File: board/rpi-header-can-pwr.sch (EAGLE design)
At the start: 64 parts, among them J1 U.FL, U1 MCP2515, U2 ADS1015, U3 BME280, U4 RFM69HCW, X2 RASPI_BOARD_B+#_E3

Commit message: fixing minor board issues
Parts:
- removed F2: FUSELITTLEFUSE, fuse:FUSELITTLEFUSE
- added F5: FUSETE5, fuse:FUSETE5
- C11, C5, C7: device rcl:C-EUC1206 -> rcl:C-EUC0805
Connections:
- net 5V: now also F5.1; no longer F2.2
- net N$8: now also F5.2; no longer F2.1

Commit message: add in219
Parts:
- removed C13: 100n, rcl:C-EUC0603
- removed C29: 10nF, eagle-ltspice:CC0603
- removed D7: BAS70-04, diode:BAS70-04
- removed R10: 4.7K, resistor:R-EU_R0603
- removed R20: 68k, rcl:R-EU_R0603
- removed R21: 20k, rcl:R-EU_R0603
- removed R22: 1k, rcl:R-EU_R0603
- removed R7: 0, resistor:R-EU_R0603
- removed U2: ADS1015, SparkFun-IC-Conversion:ADS1015
- added C18: 100n, rcl:C-EUC0603
- added R12, R13: 10K, microbuilder:RESISTOR0603
- added R19: 0.1/1% (PT2512FK-070R1L), microbuilder:RESISTOR2512
- added U5: INA219BIDCNT, microbuilder:INA219
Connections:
- removed net 12V_REFERENCE4: D7.C1A2, R20.2, R21.2, R22.1
- removed net ADC_ALERT: R7.1, X2.GPIO21
- removed net ADC_INPUT_1: C29.2, R22.2, U2.AIN0
- removed net N$9: R10.1, R7.2, U2.ALERT/RDY
- new net N$15: R13.2, U5.A1
- new net N$16: R12.2, U5.A0
- new net PRE_SENSE_12V: J3.1, R19.2, U5.VIN+
- new net SCL: U5.SCL
- new net SDA: U5.SDA
- net +12V: no longer R20.1
- net +3V3: now also C18.1, U5.VCC; no longer C13.1, D7.C2, R10.2, U2.VDD
- net GND: now also C18.2, R12.1, R13.1, U5.GND; no longer C13.2, C29.1, D7.A1, R21.1, U2.ADDR, U2.VSS
- net I2C_SCL: no longer U2.SCL
- net I2C_SDA: no longer U2.SDA
- net LORA_DIO0: now also X2.GPIO24; no longer X2.GPIO22
- net LORA_DIO2: now also X2.GPIO22; no longer X2.GPIO24
- net LORA_RST: now also X2.GPIO16; no longer X2.GPIO25
- net PRE_FUSE_12V: now also R19.1, U5.VIN-; no longer J3.1

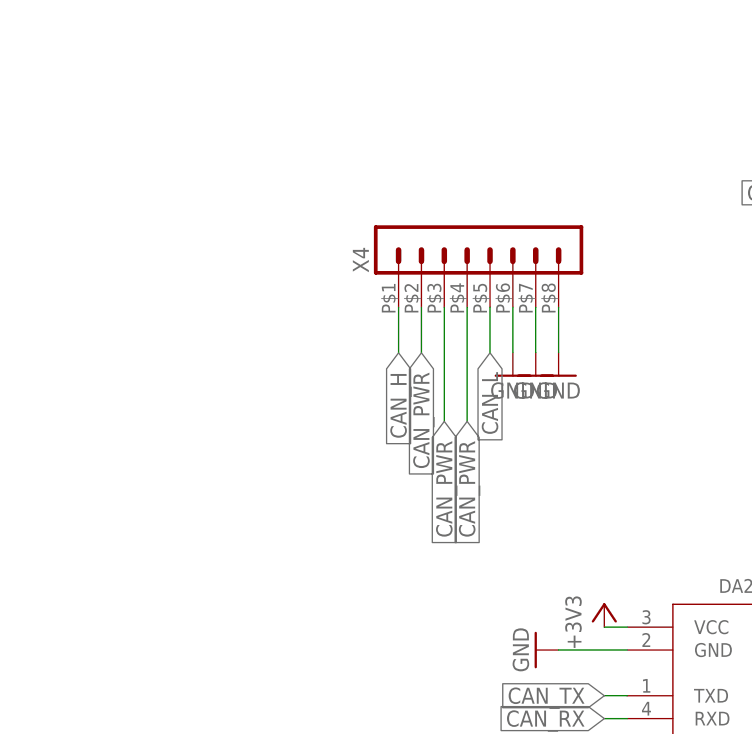
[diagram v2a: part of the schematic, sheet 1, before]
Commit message: change back to rj45 (from microfit)
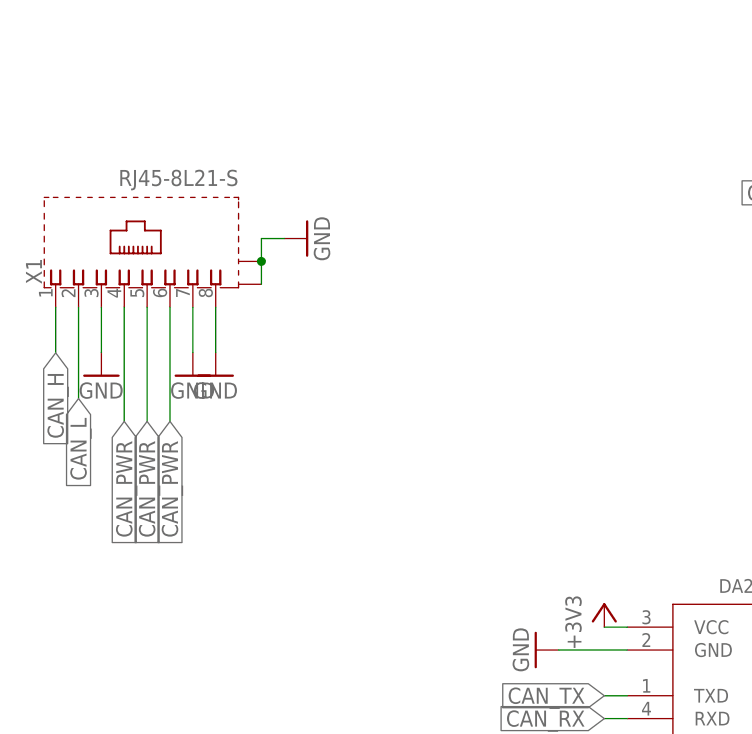
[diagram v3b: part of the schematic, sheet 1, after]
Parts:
- removed X4: (no value), con-molex-micro-fit-3_0:HEADER_POS8_43045-0812
- added X1: RJ45-8L21-S, con-tycoelectronics:RJ45-8L21-S
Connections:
- net CAN_H: now also X1.1; no longer X4.1
- net CAN_L: now also X1.2; no longer X4.5
- net CAN_PWR: now also X1.4, X1.5, X1.6; no longer X4.2, X4.3, X4.4
- net GND: now also X1.3, X1.7, X1.8, X1.S@1, X1.S@2; no longer X4.6, X4.7, X4.8
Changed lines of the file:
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@@
 <part name="C14" library="rcl" deviceset="C-EU" device="C0603" value="1u"/>
 <part name="C15" library="rcl" deviceset="C-EU" device="C0603" value="100n"/>
-<part name="GND23" library="supply1" deviceset="GND" device=""/>
-<part name="GND26" library="supply1" deviceset="GND" device=""/>
-<part name="X4" library="con-molex-micro-fit-3_0" deviceset="HEADER_POS8_?" device="43045-0812"/>
-<part name="GND29" library="supply1" deviceset="GND" device=""/>
 <part name="R11" library="rcl" deviceset="R-EU_" device="R0603" value="120"/>
 <part name="GND17" library="supply1" deviceset="GND" device=""/>
@@
 <part name="C18" library="rcl" deviceset="C-EU" device="C0603" value="100n"/>
 <part name="+3V18" library="supply1" deviceset="+3V3" device=""/>
+<part name="X1" library="con-tycoelectronics" deviceset="RJ45*2" device="1-S" technology="-8L"/>
+<part name="GND28" library="supply1" deviceset="GND" device=""/>
+<part name="GND30" library="supply1" deviceset="GND" device=""/>
+<part name="GND3" library="supply1" deviceset="GND" device=""/>
+<part name="GND19" library="supply1" deviceset="GND" device=""/>
 </parts>
 <sheets>
@@
 <instance part="GND22" gate="1" x="142.24" y="10.16" rot="R90"/>
 <instance part="+3V9" gate="G$1" x="142.24" y="22.86" rot="R270"/>
-<instance part="GND23" gate="1" x="-119.38" y="-20.32"/>
-<instance part="GND26" gate="1" x="-116.84" y="-20.32"/>
-<instance part="X4" gate="G$1" x="-124.46" y="-7.62" rot="R90"/>
-<instance part="GND29" gate="1" x="-121.92" y="-20.32"/>
 <instance part="R11" gate="G$1" x="-76.2" y="0" rot="R180"/>
+<instance part="X1" gate="G$1" x="-162.56" y="-5.08" rot="R90"/>
+<instance part="GND28" gate="1" x="-167.64" y="-20.32"/>
+<instance part="GND30" gate="1" x="-157.48" y="-20.32"/>
+<instance part="GND3" gate="1" x="-154.94" y="-20.32"/>
+<instance part="GND19" gate="1" x="-144.78" y="-5.08" rot="R90"/>
 </instances>
 <busses>
@@
 </segment>
 <segment>
-<wire x1="-119.38" y1="-12.7" x2="-119.38" y2="-17.78" width="0.1524" layer="91"/>
-<pinref part="GND23" gate="1" pin="GND"/>
-<pinref part="X4" gate="G$1" pin="7"/>
-</segment>
-<segment>
-<wire x1="-116.84" y1="-12.7" x2="-116.84" y2="-17.78" width="0.1524" layer="91"/>
-<pinref part="GND26" gate="1" pin="GND"/>
-<pinref part="X4" gate="G$1" pin="8"/>
-</segment>
-<segment>
-<pinref part="X4" gate="G$1" pin="6"/>
-<wire x1="-121.92" y1="-12.7" x2="-121.92" y2="-17.78" width="0.1524" layer="91"/>
-<pinref part="GND29" gate="1" pin="GND"/>
+<pinref part="X1" gate="G$1" pin="3"/>
+<wire x1="-167.64" y1="-12.7" x2="-167.64" y2="-17.78" width="0.1524" layer="91"/>
+<pinref part="GND28" gate="1" pin="GND"/>
+</segment>
+<segment>
+<pinref part="X1" gate="G$1" pin="7"/>
+<wire x1="-157.48" y1="-12.7" x2="-157.48" y2="-17.78" width="0.1524" layer="91"/>
+<pinref part="GND30" gate="1" pin="GND"/>
+</segment>
+<segment>
+<pinref part="X1" gate="G$1" pin="8"/>
+<wire x1="-154.94" y1="-12.7" x2="-154.94" y2="-17.78" width="0.1524" layer="91"/>
+<pinref part="GND3" gate="1" pin="GND"/>
+</segment>
+<segment>
+<pinref part="X1" gate="G$1" pin="S@1"/>
+<pinref part="X1" gate="G$1" pin="S@2"/>
+<wire x1="-149.86" y1="-10.16" x2="-149.86" y2="-7.62" width="0.1524" layer="91"/>
+<wire x1="-149.86" y1="-7.62" x2="-149.86" y2="-5.08" width="0.1524" layer="91"/>
+<junction x="-149.86" y="-7.62"/>
+<wire x1="-149.86" y1="-5.08" x2="-147.32" y2="-5.08" width="0.1524" layer="91"/>
+<pinref part="GND19" gate="1" pin="GND"/>
 </segment>
 </net>
@@
 </segment>
 <segment>
-<wire x1="-134.62" y1="-12.7" x2="-134.62" y2="-17.78" width="0.1524" layer="91"/>
-<label x="-134.62" y="-17.78" size="1.778" layer="95" rot="R270" xref="yes"/>
-<pinref part="X4" gate="G$1" pin="1"/>
-</segment>
-<segment>
 <pinref part="R11" gate="G$1" pin="2"/>
 <wire x1="-81.28" y1="0" x2="-86.36" y2="0" width="0.1524" layer="91"/>
 <label x="-86.36" y="0" size="1.778" layer="95" rot="R180" xref="yes"/>
 </segment>
+<segment>
+<pinref part="X1" gate="G$1" pin="1"/>
+<wire x1="-172.72" y1="-12.7" x2="-172.72" y2="-17.78" width="0.1524" layer="91"/>
+<label x="-172.72" y="-17.78" size="1.778" layer="95" rot="R270" xref="yes"/>
+</segment>
 </net>
 <net name="CAN_L" class="0">
@@
 </segment>
 <segment>
-<pinref part="X4" gate="G$1" pin="5"/>
-<wire x1="-124.46" y1="-12.7" x2="-124.46" y2="-17.78" width="0.1524" layer="91"/>
-<label x="-124.46" y="-17.78" size="1.778" layer="95" rot="R270" xref="yes"/>
-</segment>
-<segment>
 <pinref part="R11" gate="G$1" pin="1"/>
 <wire x1="-66.04" y1="0" x2="-71.12" y2="0" width="0.1524" layer="91"/>
 <label x="-66.04" y="0" size="1.778" layer="95" xref="yes"/>
 </segment>
+<segment>
+<pinref part="X1" gate="G$1" pin="2"/>
+<wire x1="-170.18" y1="-12.7" x2="-170.18" y2="-22.86" width="0.1524" layer="91"/>
+<label x="-170.18" y="-22.86" size="1.778" layer="95" rot="R270" xref="yes"/>
+</segment>
 </net>
 <net name="N$17" class="0">
@@
 <net name="CAN_PWR" class="0">
 <segment>
-<pinref part="X4" gate="G$1" pin="2"/>
-<wire x1="-132.08" y1="-12.7" x2="-132.08" y2="-17.78" width="0.1524" layer="91"/>
-<label x="-132.08" y="-17.78" size="1.778" layer="95" rot="R270" xref="yes"/>
-</segment>
-<segment>
-<pinref part="X4" gate="G$1" pin="3"/>
-<wire x1="-129.54" y1="-12.7" x2="-129.54" y2="-25.4" width="0.1524" layer="91"/>
-<label x="-129.54" y="-25.4" size="1.778" layer="95" rot="R270" xref="yes"/>
-</segment>
-<segment>
-<wire x1="-127" y1="-12.7" x2="-127" y2="-25.4" width="0.1524" layer="91"/>
-<label x="-127" y="-25.4" size="1.778" layer="95" rot="R270" xref="yes"/>
-<pinref part="X4" gate="G$1" pin="4"/>
-</segment>
-<segment>
 <label x="-25.4" y="12.7" size="1.778" layer="95" rot="R180" xref="yes"/>
 <pinref part="F3" gate="G$1" pin="1"/>
 <wire x1="-25.4" y1="12.7" x2="-15.24" y2="12.7" width="0.1524" layer="91"/>
 </segment>
-</net>
+<segment>
+<pinref part="X1" gate="G$1" pin="4"/>
+<wire x1="-165.1" y1="-12.7" x2="-165.1" y2="-25.4" width="0.1524" layer="91"/>
+<label x="-165.1" y="-25.4" size="1.778" layer="95" rot="R270" xref="yes"/>
+</segment>
+<segment>
+<pinref part="X1" gate="G$1" pin="5"/>
+<wire x1="-162.56" y1="-12.7" x2="-162.56" y2="-25.4" width="0.1524" layer="91"/>
+<label x="-162.56" y="-25.4" size="1.778" layer="95" rot="R270" xref="yes"/>
+</segment>
+<segment>
+<pinref part="X1" gate="G$1" pin="6"/>
+<wire x1="-160.02" y1="-12.7" x2="-160.02" y2="-25.4" width="0.1524" layer="91"/>
+<label x="-160.02" y="-25.4" size="1.778" layer="95" rot="R270" xref="yes"/>
+</segment>
+</net>

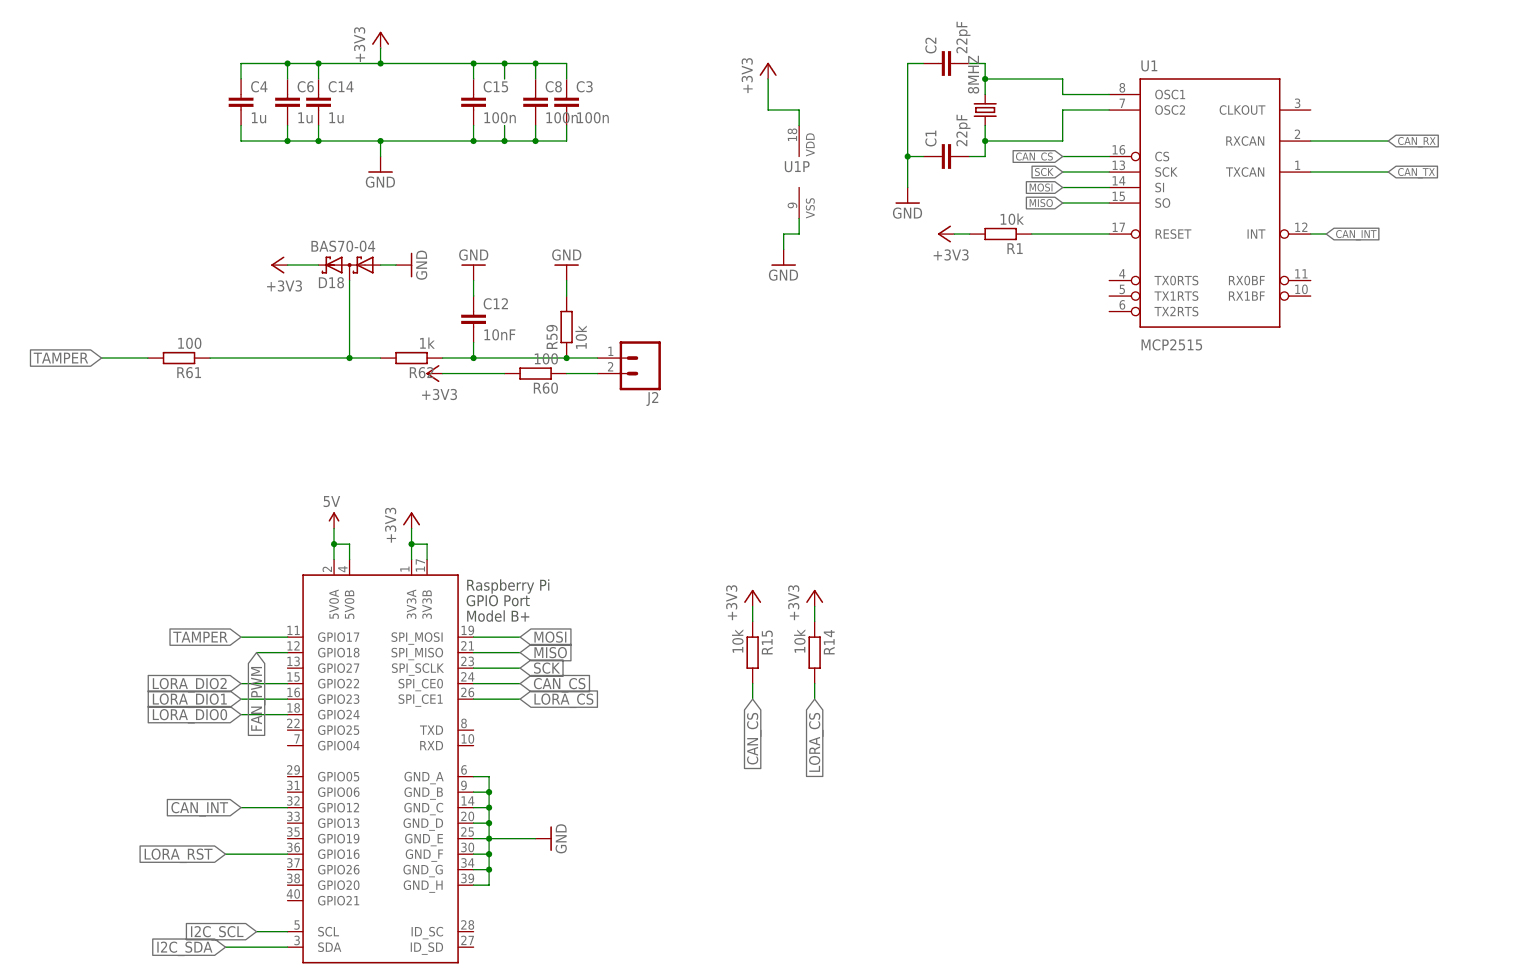
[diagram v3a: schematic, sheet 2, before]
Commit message: replace components with ones that has place drawing
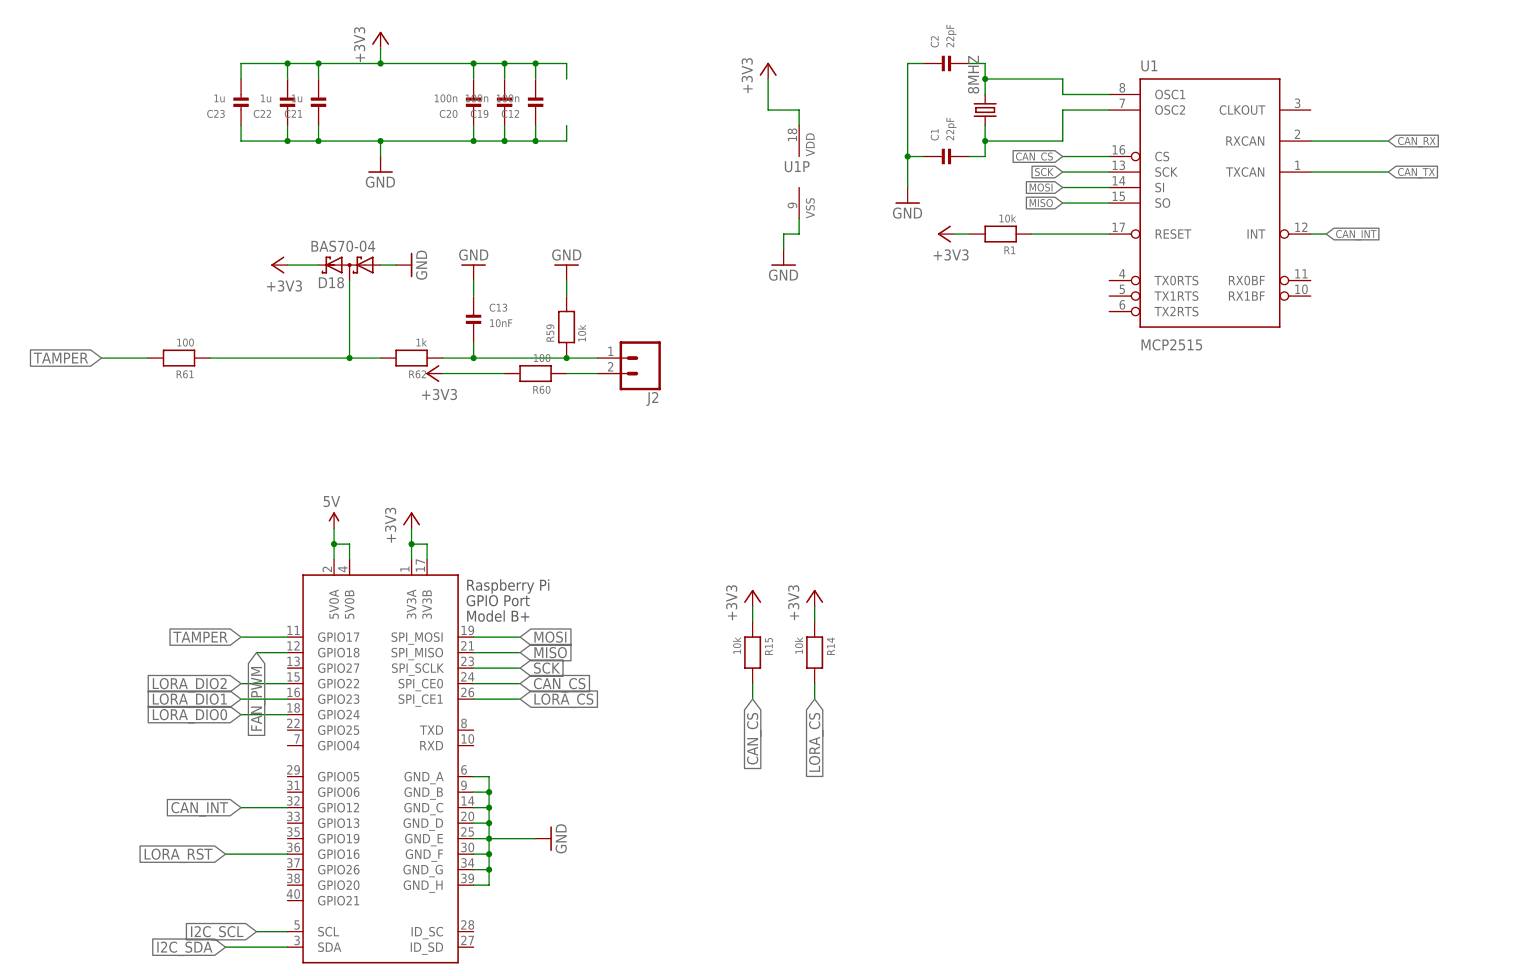
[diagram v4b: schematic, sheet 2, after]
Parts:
- removed C10: 100n, rcl:C-EUC0805
- removed C11, C5, C7: 22uF, rcl:C-EUC0805
- removed C18: 100n, rcl:C-EUC0603
- removed C9: 4,7u, rcl:C-EUC0805
- removed J3: (no value), SparkFun-Connectors:CONN_025MM
- removed T2: (no value), zetex:NPNSOT23
- added C13: 10nF, microbuilder:CAP_CERAMIC0603
- added C19, C20: 100n, microbuilder:CAP_CERAMIC0603
- added C21, C22, C23: 1u, microbuilder:CAP_CERAMIC0603
- added J4: (no value), SparkFun-Connectors:CONN_025MM
- added Q3: (no value), microbuilder:TRANSISTOR_NPNWIDE
- C1, C2: device SparkFun-Capacitors:22PF-50V-5%(0603) -> microbuilder:CAP_CERAMIC0603
- C12: value 10nF -> 100n; device eagle-ltspice:CC0603 -> microbuilder:CAP_CERAMIC0603
- C14: value 1u -> 22uF; device rcl:C-EUC0603 -> microbuilder:CAP_CERAMIC0805
- C15, C8: value 100n -> 22uF; device rcl:C-EUC0603 -> microbuilder:CAP_CERAMIC0805
- C16: device microbuilder:CAP_CERAMIC0603_NO -> microbuilder:CAP_CERAMIC0603
- C17: device microbuilder:CAP_CERAMIC0805-NOOUTLINE -> microbuilder:CAP_CERAMIC0603
- C3: device rcl:C-EUC0603 -> microbuilder:CAP_CERAMIC0603
- C4: value 1u -> 4,7u; device rcl:C-EUC0603 -> microbuilder:CAP_CERAMIC0805
- C6: value 1u -> 100n; device rcl:C-EUC0603 -> microbuilder:CAP_CERAMIC0805
- D3: value BC846 -> (none); device transistor:BC846 -> microbuilder:TRANSISTOR_NPNWIDE
- R1, R11, R14, R15, R17, R2, R24, R3, R4, R5, R59, R60, R61, R62: device rcl:R-EU_R0603 -> microbuilder:RESISTOR0603
- R12, R13: value 10K -> 1K
- R8, R9: device resistor:R-EU_R0603 -> microbuilder:RESISTOR0603
- renumbered R6 to R7
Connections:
- net +12V: now also C4.P$1, C6.P$1; no longer C10.1, C9.1
- net +3V3: now also C12.P$2, C16.P$1, C17.P$1, C19.P$2, C20.P$2, C21.P$2, C22.P$2, C23.P$2, C3.P$1; no longer C14.1, C15.1, C16.1, C17.1, C18.1, C3.1, C4.1, C6.1, C8.1
- net GND: now also C1.P$1, C12.P$1, C13.P$1, C14.P$2, C15.P$2, C16.P$2, C17.P$2, C19.P$1, C2.P$1, C20.P$1, C21.P$1, C22.P$1, C23.P$1, C3.P$2, C4.P$2, C6.P$2, C8.P$2, J4.1, Q3.E; no longer C1.1, C10.2, C11.2, C12.1, C14.2, C15.2, C16.2, C17.2, C18.2, C2.1, C3.2, C4.2, C5.2, C6.2, C7.2, C8.2, C9.2, J3.2, T2.E
- net N$11: now also C13.P$2; no longer C12.2
- net N$12: now also Q3.B; no longer T2.B
- net N$14: now also Q3.C; no longer T2.C
- net N$2: now also C2.P$2; no longer C2.2
- net N$3: now also C1.P$2; no longer C1.2
- net N$8: now also C14.P$1, C15.P$1, C8.P$1; no longer C11.1, C5.1, C7.1
- net PRE_SENSE_12V: now also J4.2; no longer J3.1
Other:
- moved on the sheet: C12
